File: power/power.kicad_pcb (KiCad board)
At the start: 4 copper layers, 73.7 x 39.4 mm, 74 parts, among them M1 HIP2101, M2 HIP2101, M3 HIP2101, M4 ACS711, M5 ACS711, P1 PLS_10, P3 C, P4 A, P5 B, P6 VDD, P7 GND, P8 PLS_3, P9 PLS_3, Q1 CSD18532, Q2 CSD18532, Q3 CSD18532, Q4 CSD18532, Q5 CSD18532, Q6 CSD18532

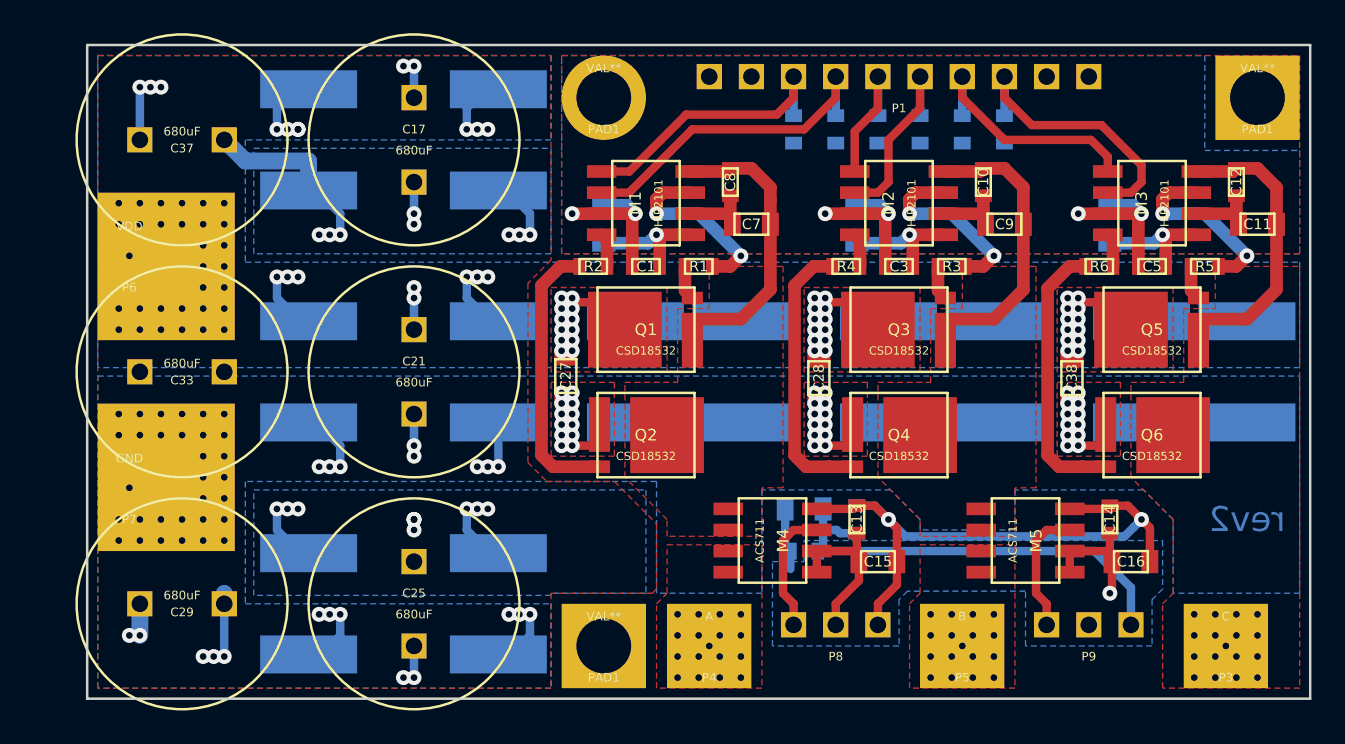
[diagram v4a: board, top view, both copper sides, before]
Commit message: Reduced decoupling capacitor bank like ESC, also added two row of pins, small fixes.
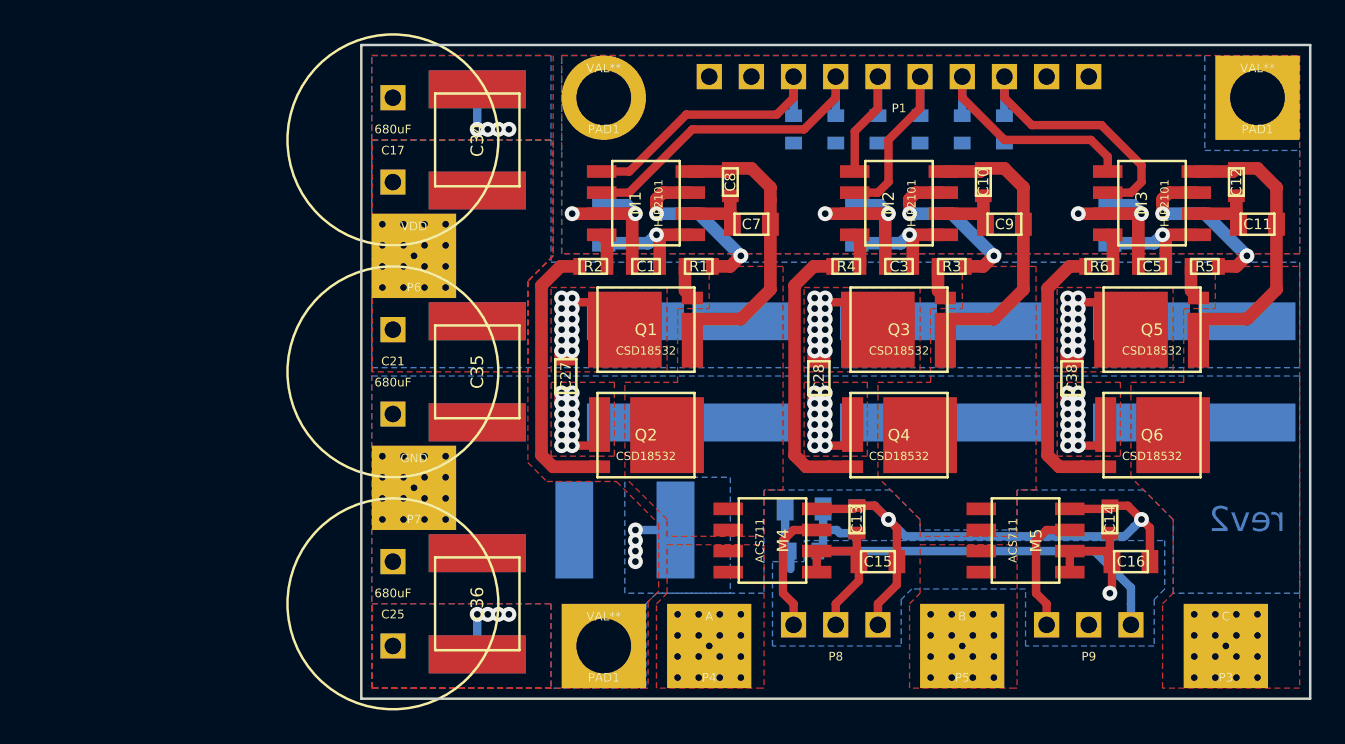
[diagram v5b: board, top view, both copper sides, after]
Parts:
- removed C33, C37: 680uF, foot:CE135
- C29: value 680uF -> 4.7uF; footprint foot:CE135 -> foot:SM2220; moved to B.Cu
- C34, C35, C36: moved to F.Cu
- moved C29 27.0 mm to (154.9, 111.1), turned to 180 degrees
- moved P6 17.1 mm to (142.2, 94.6)
- moved P7 17.1 mm to (142.2, 108.6)
- moved C34 10.2 mm to (146.1, 87.6), turned to 90 degrees
- moved C35 10.2 mm to (146.1, 101.6)
- moved C36 10.2 mm to (146.1, 115.6), turned to 90 degrees
- moved C17 1.27 mm to (141.0, 87.6), turned to 90 degrees
- moved C21 1.27 mm to (141.0, 101.6)
- moved C25 1.27 mm to (141.0, 115.6), turned to 90 degrees
- moved C18 1.27 mm to (146.1, 101.6)
- moved C31 1.27 mm to (146.1, 87.6), turned to 90 degrees
- moved C32 1.27 mm to (146.1, 115.6), turned to 90 degrees
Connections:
- P9 pad 2: Net-(P9-Pad2) -> AGND
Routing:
- net PGND: track 139.2 -> 76.8 mm, vias 99 -> 62
- net +36V: track 137.9 -> 83.7 mm, vias 97 -> 60
- net (no net): track 0.63 -> 0.00 mm
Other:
- board size 73.7 x 39.4 mm -> 57.2 x 39.4 mm

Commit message: Renew annotaion of power board, minor fixes.
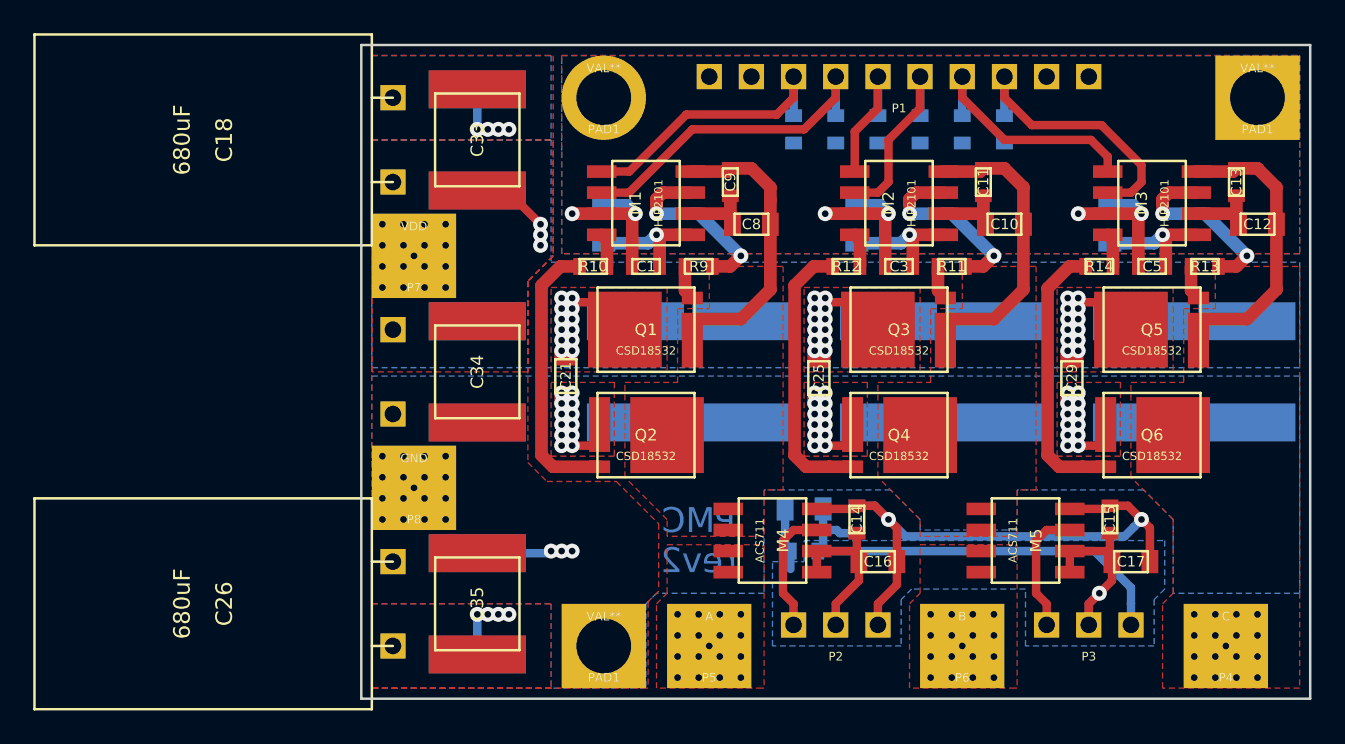
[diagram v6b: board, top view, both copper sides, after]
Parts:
- removed the C17 at (141.0, 87.6)
- removed the C21 at (141.0, 101.6)
- removed the C25 at (141.0, 115.6)
- removed the C29 at (154.9, 111.1)
- added C18: 680uF, foot:CE135L, F.Cu at (141.0, 87.6)
- added C22: 680uF, foot:CE135L, B.Cu at (141.0, 101.6)
- added C26: 680uF, foot:CE135L, F.Cu at (141.0, 115.6)
- R10: renamed from R2; value 1 -> 2
- R11: renamed from R3; value 1 -> 2
- R12: renamed from R4; value 1 -> 2
- R13: renamed from R5; value 1 -> 2
- R14: renamed from R6; value 1 -> 2
- R9: renamed from R1; value 1 -> 2
- renumbered C9 to C10, C10 to C11, C11 to C12, C12 to C13, C13 to C14, C14 to C15, C15 to C16, C16 to C17, C18 to C19, C19 to C20, C27 to C21, C22 to C23, C23 to C24, C28 to C25, C20 to C27, C24 to C28, C38 to C29, C34 to C33, C35 to C34, C36 to C35, C26 to C7, C7 to C8, C8 to C9, P8 to P2, P9 to P3, P3 to P4, P4 to P5, P5 to P6, P6 to P7, P7 to P8, R9 to R1, R10 to R2, R11 to R3, R12 to R4, R13 to R5, R14 to R6
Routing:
- net PGND: track 76.8 -> 82.6 mm, vias 62 -> 65
- net AGND: track 20.8 -> 25.4 mm
- net +36V: track 83.7 -> 85.3 mm, vias 60 -> 59
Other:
- board text added: "PMC rev2"
- board text removed: "rev2"
